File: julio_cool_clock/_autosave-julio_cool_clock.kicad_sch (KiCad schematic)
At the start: 42 parts, among them J1 PJ-102AH, J2 Conn_01x06, J2 Conn_02x03_Odd_Even, SW1 Omron_B3F_SPST, SW2 Omron_B3F_SPST, SW3 Omron_B3F_SPST, SW4 Omron_B3F_SPST, U1 ATmega328-PU, U2 MAX7219, U3 DS1307_DIP-8, U4 L7805, Y1 Crystal_16MHz, Y2 Crystal_32768Hz

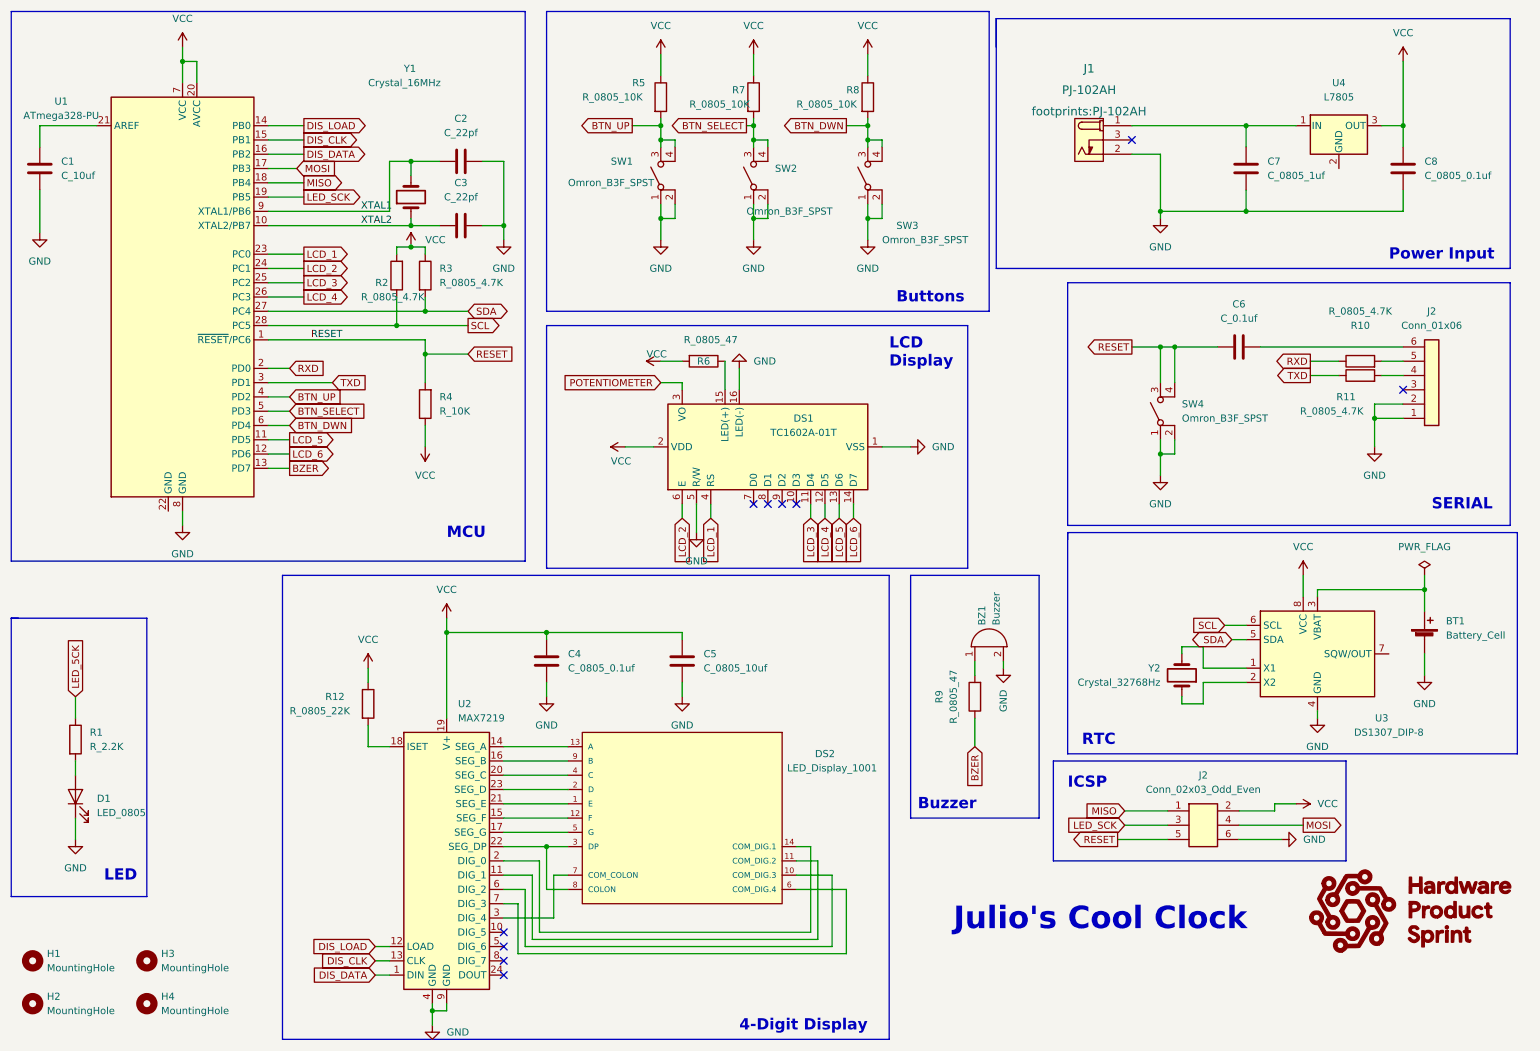
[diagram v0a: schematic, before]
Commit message: Design Commit 4.2
Arranged components from schematic onto PCB.
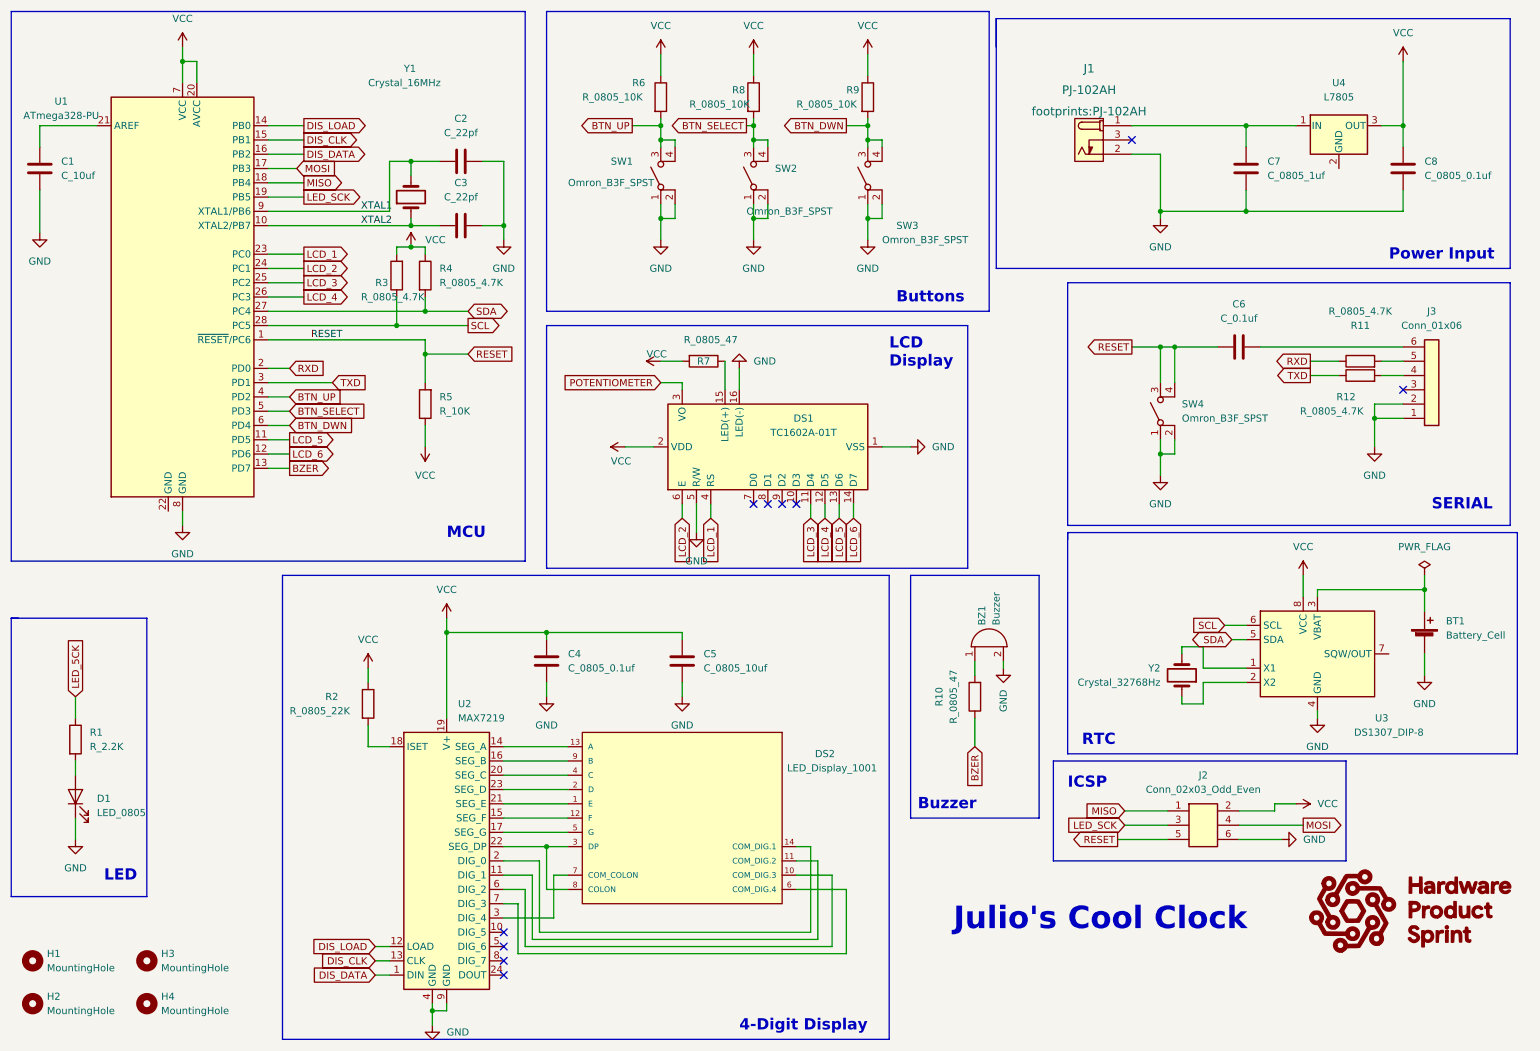
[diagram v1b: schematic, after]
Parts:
- renumbered J2 to J3, R9 to R10, R10 to R11, R11 to R12, R12 to R2, R2 to R3, R3 to R4, R4 to R5, R5 to R6, R6 to R7, R7 to R8, R8 to R9
